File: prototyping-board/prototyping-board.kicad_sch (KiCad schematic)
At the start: 45 parts, among them J1 Conn_01x02, J10 Conn_01x02, J11 Conn_01x03, J12 Conn_01x03, J13 Conn_01x03, J14 Conn_01x03, J15 Conn_01x03, J16 Conn_01x03, J17 Conn_01x03, J18 Conn_01x03, J19 Conn_01x03, J2 Conn_01x02, J20 Conn_01x03, J21 Conn_01x03, J22 Conn_01x03, J23 Conn_01x06, J24 Conn_01x06, J25 Conn_01x04, J26 Conn_01x04, J27 Conn_01x05, J28 Conn_01x05, J29 Conn_01x05, J3 Conn_01x02, J30 Conn_01x04, J31 Conn_01x04, J32 Conn_01x04, J33 Conn_01x03, J34 Conn_01x03, J35 Conn_01x03, J36 Conn_01x02, J37 Conn_01x02, J38 Conn_01x02, J39 Conn_01x04, J4 Conn_01x02, J5 Conn_01x02, J6 Conn_01x02, J7 Conn_01x02, J8 Conn_01x02, J9 Conn_01x02, U1 MEGA_PRO_EMBED_CH340G___ATMEG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

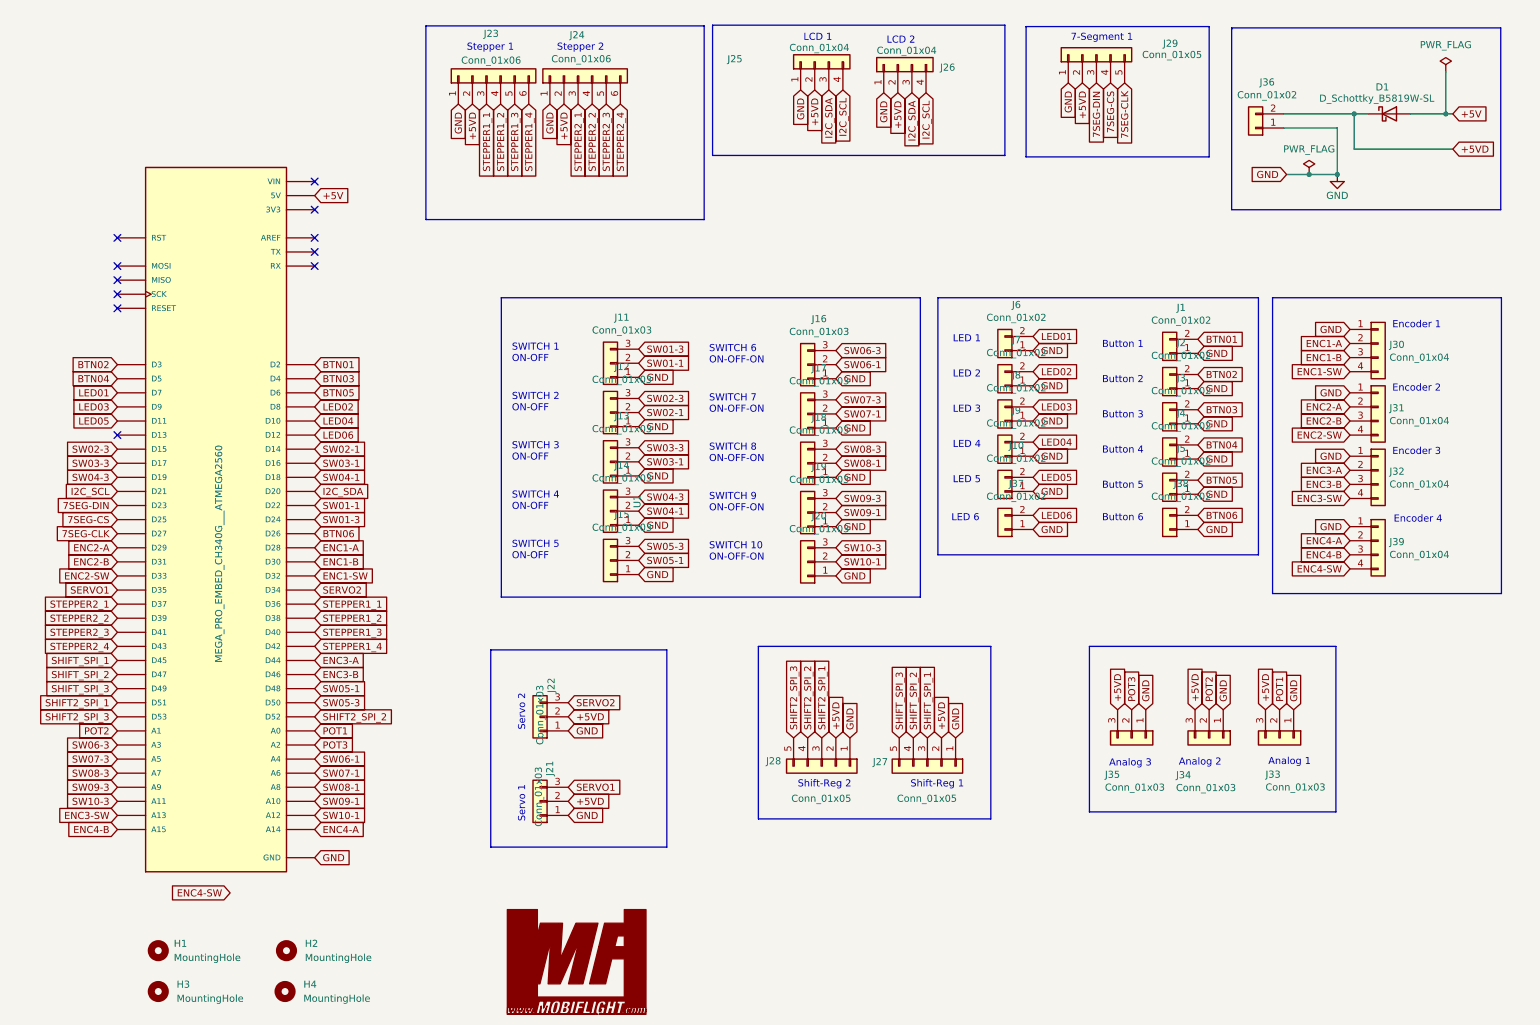
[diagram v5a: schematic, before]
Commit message: ENC4 switch to Button 6
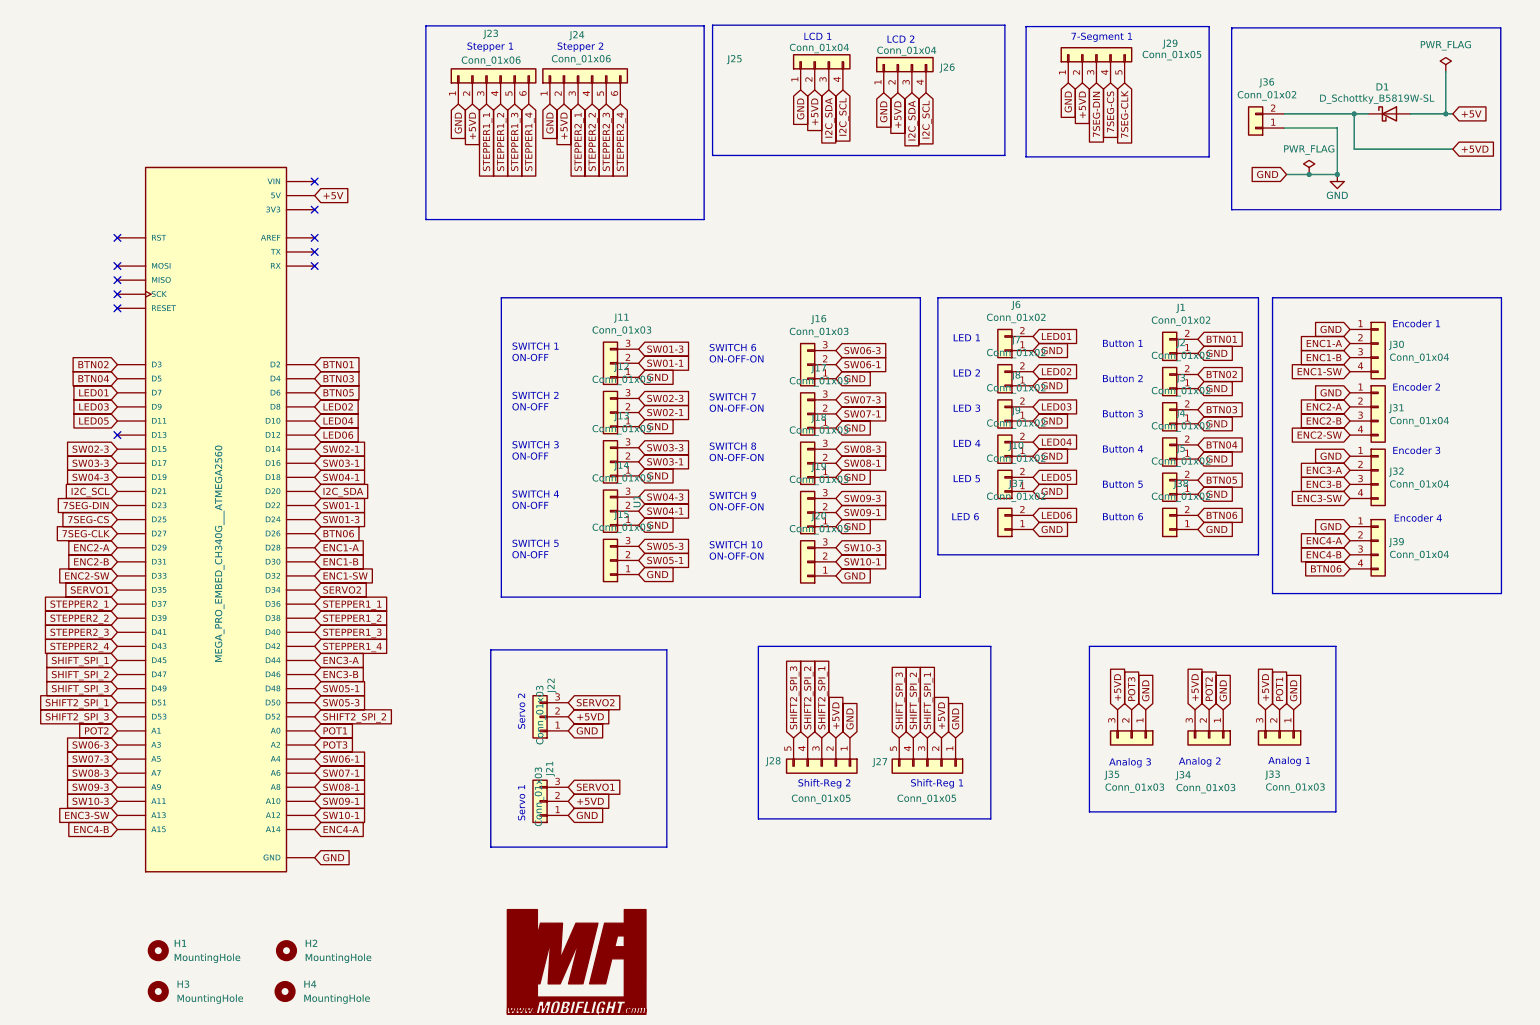
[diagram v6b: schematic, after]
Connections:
- net ENC4-SW is gone; now on net BTN06: J39.4 (Pin_4)
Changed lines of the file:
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@@
 	(title_block
 		(title "MobiFlight Prototyping Board")
-		(date "09.12.2022")
-		(rev "2.1")
+		(date "2025-11-02")
+		(rev "2.2")
 		(company "mobiflight community")
 		(comment 1 "stephan hoeltig")
@@
 		)
 	)
+	(global_label "BTN06"
+		(shape input)
+		(at 252.73 113.03 180)
+		(fields_autoplaced yes)
+		(effects
+			(font
+				(size 1.27 1.27)
+			)
+			(justify right)
+		)
+		(property "Intersheetrefs" "${INTERSHEET_REFS}"
+			(at 244.4119 113.03 0)
+			(effects
+				(font
+					(size 1.27 1.27)
+				)
+				(justify right)
+				(hide yes)
+			)
+		)
+	)
 	(global_label "+5VD"
 		(shape input)
@@
 		)
 	)
-	(global_label "ENC4-SW"
-		(shape input)
-		(at 252.73 113.03 180)
-		(fields_autoplaced yes)
-		(effects
-			(font
-				(size 1.27 1.27)
-			)
-			(justify right)
-		)
-		(property "Intersheetrefs" "${INTERSHEET_REFS}"
-			(at 241.2067 113.03 0)
-			(effects
-				(font
-					(size 1.27 1.27)
-				)
-				(justify right)
-				(hide yes)
-			)
-		)
-	)
 	(global_label "SW02-3"
 		(shape input)
@@
 				(hide yes)
 			)
-		)
-	)
-	(global_label "ENC4-SW"
-		(shape input)
-		(at 50.8 171.45 180)
-		(fields_autoplaced yes)
-		(effects
-			(font
-				(size 1.27 1.27)
-			)
-			(justify right)
-		)
-		(property "Intersheetrefs" "${INTERSHEET_REFS}"
-			(at 39.2767 171.45 0)
-			(effects
-				(font
-					(size 1.27 1.27)
-				)
-				(justify right)
-				(hide yes)
-			)

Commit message: LED6 to D13, ENC4 switch to D12
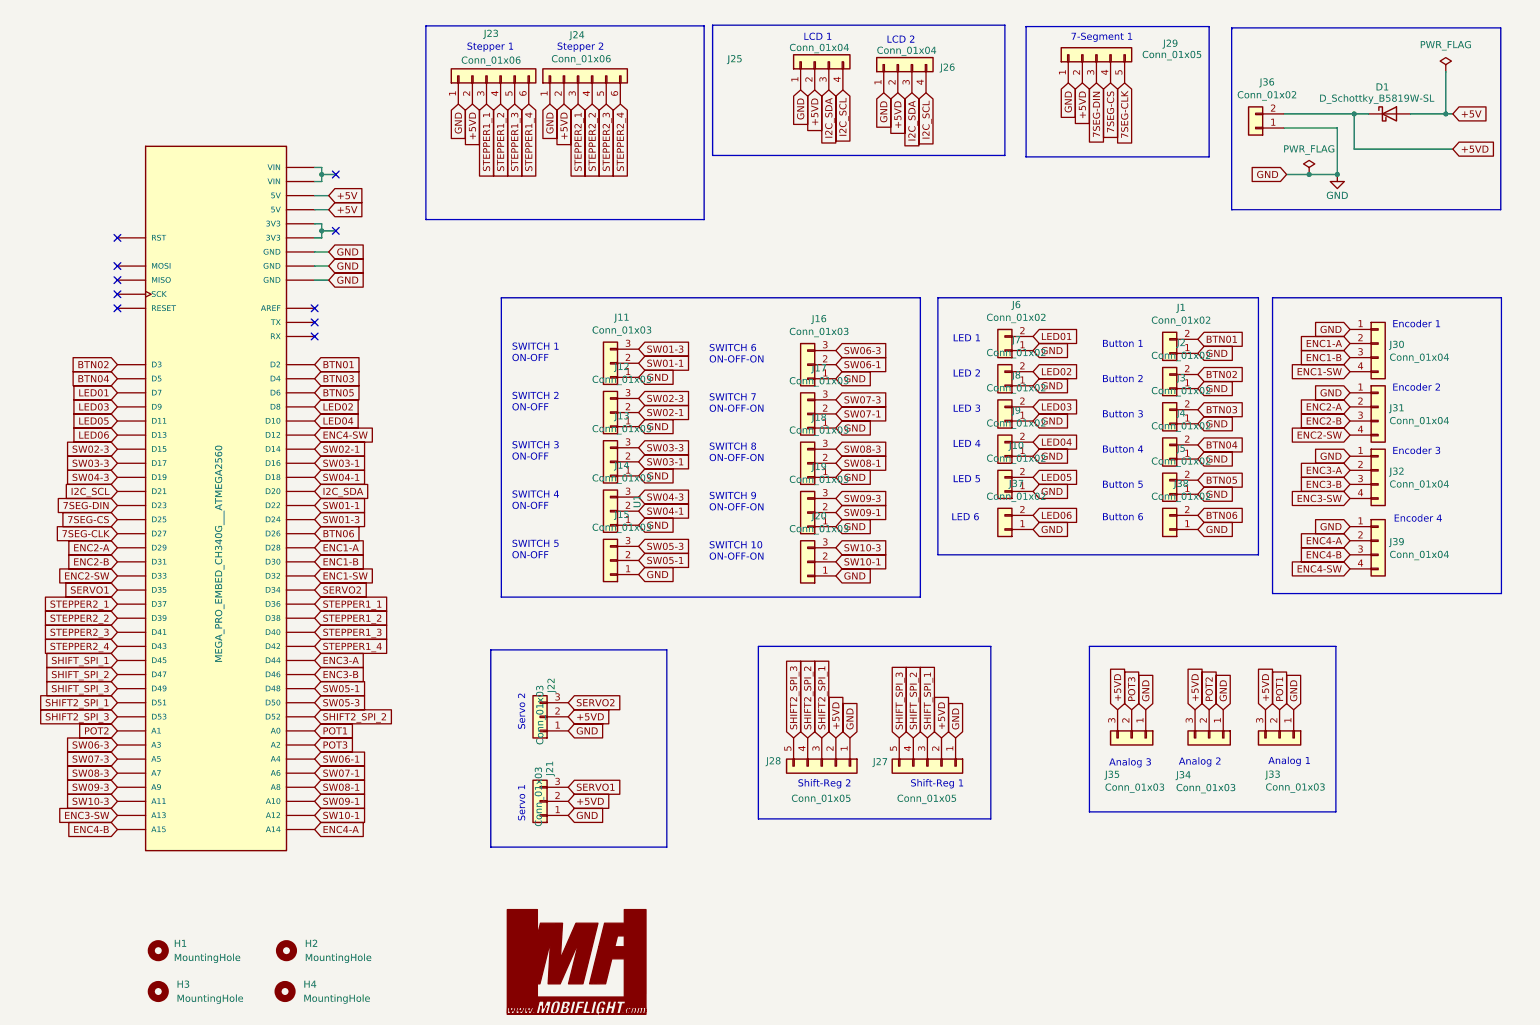
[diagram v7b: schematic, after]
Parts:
- U1: symbol mobiflight-library:MEGA_PRO_EMBED_CH340G___ATMEGA2560 -> MobiFlight:MEGA_PRO_EMBED_CH340G___ATMEGA2560
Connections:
- net +5V: no longer U1.5V_3 (5V)
- net BTN06: no longer J39.4 (Pin_4)
- net LED06: now also U1.D13; no longer U1.D12
- new net ENC4-SW: J39.4 (Pin_4), U1.D12
- no-connect marks 11 -> 10

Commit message: add a reset button, update readme accordingly
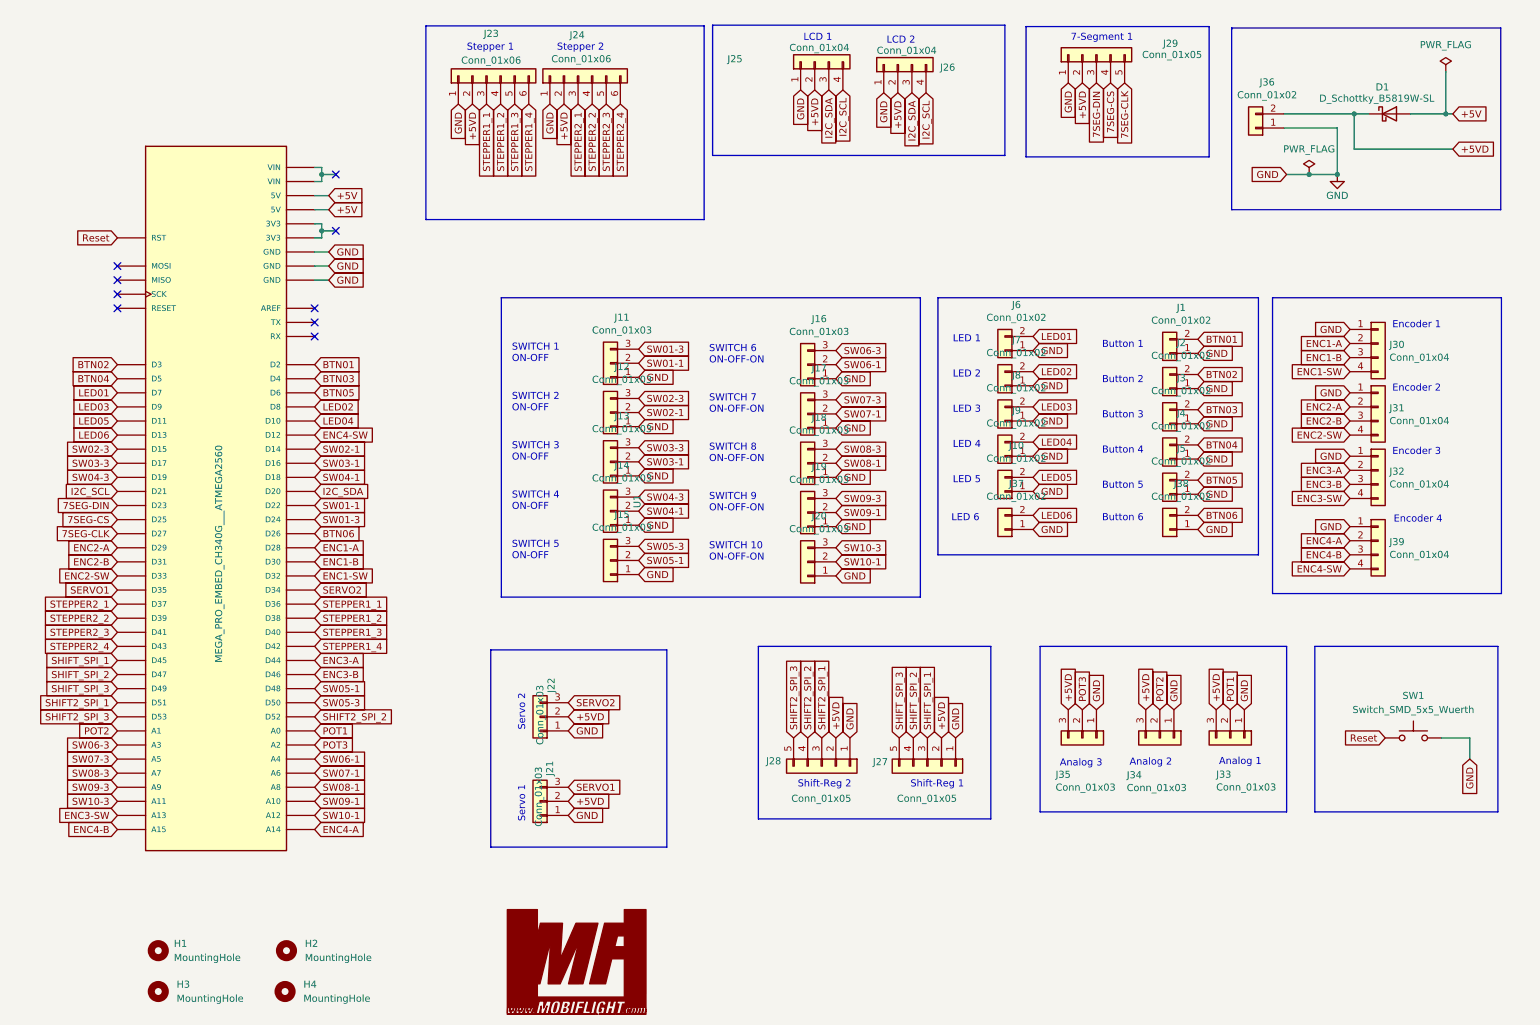
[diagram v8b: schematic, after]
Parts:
- added SW1: Switch_SMD_5x5_Wuerth, MobiFlight:SW_Push_1P1T_NO_Vertical_Wuerth_434133025816, symbol MobiFlight:Switch_SMD_5x5_Wuerth
- U1: now left out of the parts list
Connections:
- net GND: now also SW1.2
- net Reset: now reaches U1.RST
- net Reset: now also SW1.1
- no-connect marks 10 -> 9
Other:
- moved on the sheet: J33, J34, J35
